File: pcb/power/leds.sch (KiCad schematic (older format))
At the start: 26 parts, among them U4 LM324QT

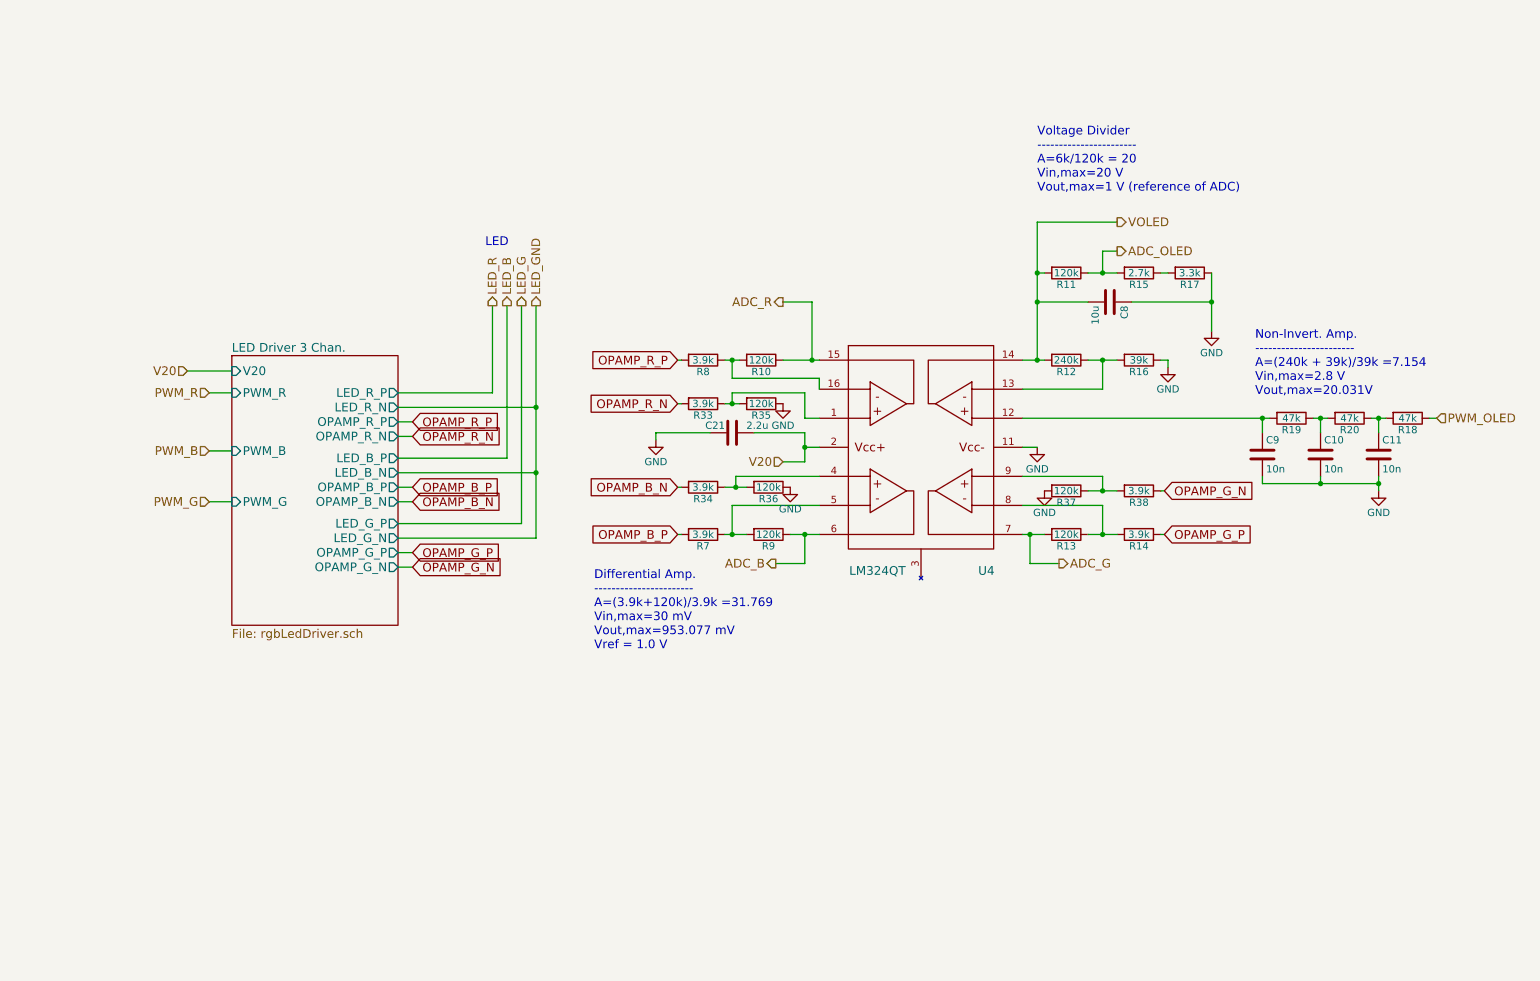
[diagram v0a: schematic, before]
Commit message: Almost finished the new schematics.
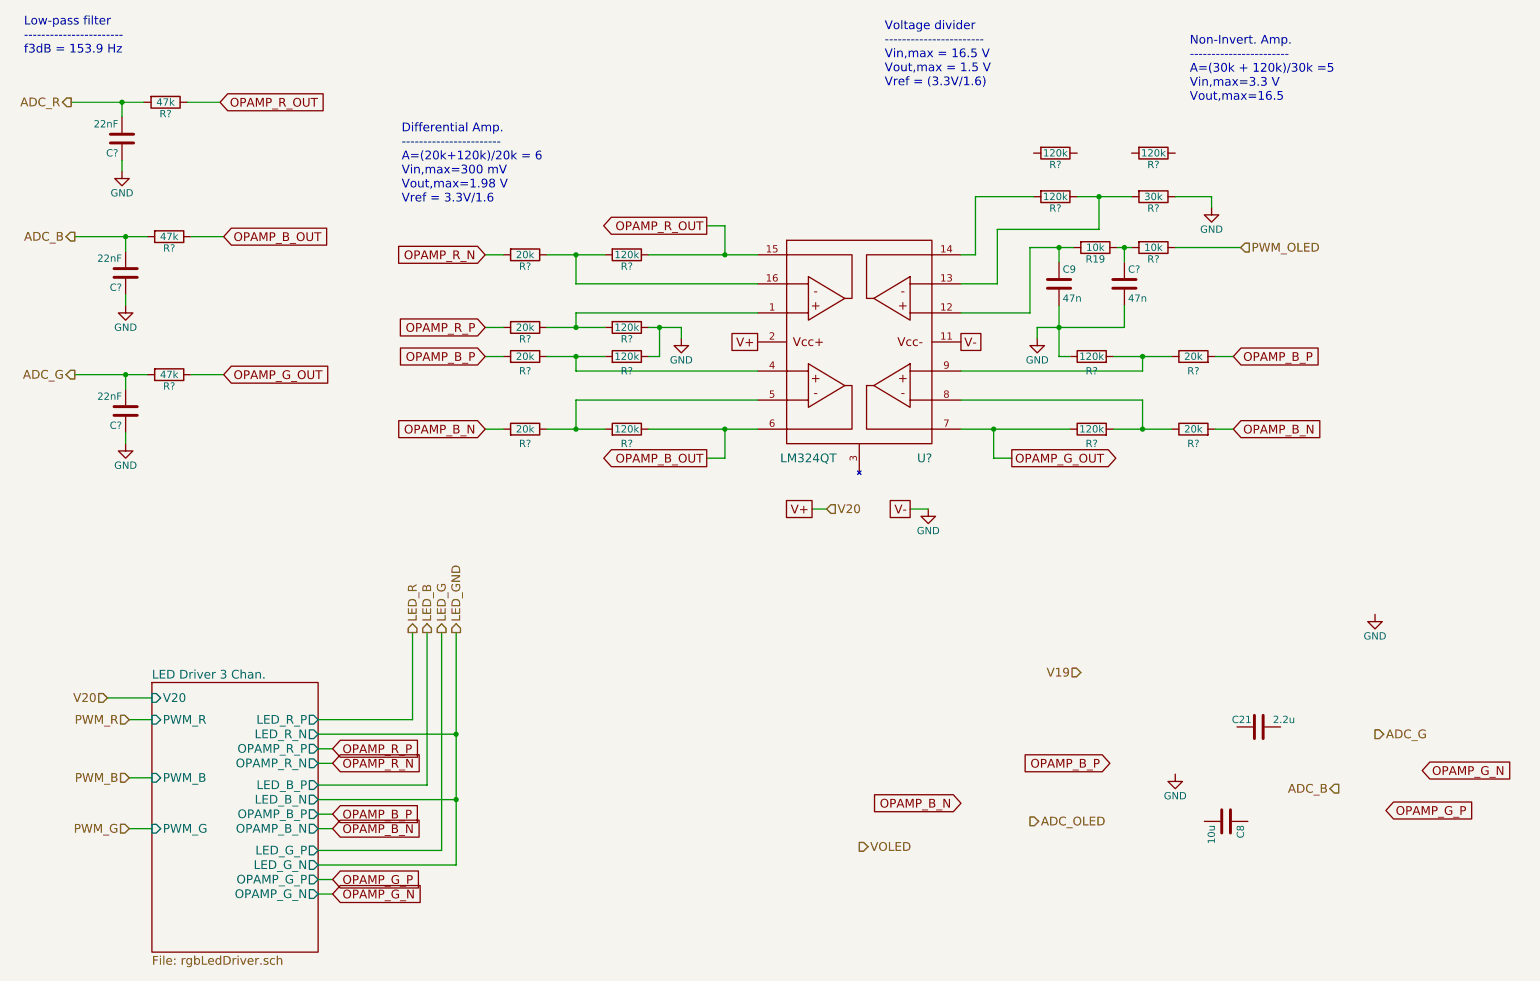
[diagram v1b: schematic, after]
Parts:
- removed C10, C11: 10n, Capacitors_SMD:C_0603_HandSoldering, symbol C
- removed R10, R11, R13, R35, R36, R37, R9: 120k, Additional:R_0603_HandSoldering_Same_As_C, symbol R
- removed R12: 240k, Additional:R_0603_HandSoldering_Same_As_C, symbol R
- removed R14, R33, R34, R38, R7, R8: 3.9k, Additional:R_0603_HandSoldering_Same_As_C, symbol R
- removed R15: 2.7k, Additional:R_0603_HandSoldering_Same_As_C, symbol R
- removed R16: 39k, Additional:R_0603_HandSoldering_Same_As_C, symbol R
- removed R17: 3.3k, Additional:R_0603_HandSoldering_Same_As_C, symbol R
- removed R18, R20: 47k, Additional:R_0603_HandSoldering_Same_As_C, symbol R
- removed U4: LM324QT, Additional:QFN-16-1EP_3x3mm_Pitch0.5mm, symbol LM324QT
- added C?: 47n, Capacitors_SMD:C_0603_HandSoldering, symbol C
- added C? (x3): 22nF, Capacitors_SMD:C_0603_HandSoldering, symbol C
- added R?: 10k, Additional:R_0603_HandSoldering_Same_As_C, symbol R
- added R? (x6): 20k, Additional:R_0603_HandSoldering_Same_As_C, symbol R
- added R? (x9): 120k, Additional:R_0603_HandSoldering_Same_As_C, symbol R
- added R? (x3): 47k, Additional:R_0603_HandSoldering_Same_As_C, symbol R
- added R?: 30k, Additional:R_0603_HandSoldering_Same_As_C, symbol R
- added U?: LM324QT, symbol LM324QT
- C9: value 10n -> 47n; Digikey 311-1085-1-ND -> (none); Farnell (none) -> 1759011
- R19: value 47k -> 10k; Digikey 311-47.0KHRCT-ND -> (none); Farnell (none) -> 2141505
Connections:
- net ADC_B: now also C?.2, R?.2
- net ADC_G: now also C?.2, R?.2
- net ADC_R: now also C?.2, R?.2
- net GND: now also C?.1, C?.1, C?.1, C?.2, R?.1, R?.1, R?.1, R?.1, U?.11 (Vcc-); no longer C21.1, C8.1
- net OPAMP_B_N: now also R?.2, R?.2
- net OPAMP_B_P: now also R?.2, R?.2
- net OPAMP_R_N: now also R?.2
- net OPAMP_R_P: now also R?.2
- net PWM_OLED: now also R?.1
- net VOLED: no longer C8.2
- net at C9.1, R19.2: now also U?.12 (P_4)
- net at R19.1: now also C?.1, R?.2
- net V20: no longer names the net of C21.2
- new net: R?.1, R?.2, U?.1 (P_1)
- new net: R?.1, R?.2, U?.13 (N_4)
- new net: R?.2, U?.14 (O_4)
- new net: R?.1, R?.2, U?.16 (N_1)
- new net: R?.1, R?.2, U?.4 (P_2)
- new net: R?.1, R?.2, U?.5 (N_2)
- new net: R?.1, R?.2, U?.8 (N_3)
- new net: R?.1, R?.2, U?.9 (P_3)
- new net OPAMP_B_OUT: R?.1, R?.1, U?.6 (O_2)
- new net OPAMP_G_OUT: R?.1, R?.1, U?.7 (O_3)
- new net OPAMP_R_OUT: R?.1, R?.1, U?.15 (O_1)
- new net V+: U?.2 (Vcc+)
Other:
- note added: "Differential Amp.\n-----------------------\nA=(20k+120k)/20k = 6\nVin,max=300 mV\nVout,max=1.98 V\nVref = 3.3V/1.6"
- note added: "Low-pass filter\n-----------------------\nf3dB = 153.9 Hz"
- note added: "Non-Invert. Amp.\n-----------------------\nA=(30k + 120k)/30k =5\nVin,max=3.3 V\nVout,max=16.5"
- note added: "Voltage divider\n-----------------------\nVin,max = 16.5 V\nVout,max = 1.5 V \nVref = (3.3V/1.6)"
- note removed: "Differential Amp.\n-----------------------\nA=(3.9k+120k)/3.9k =31.769\nVin,max=30 mV\nVout,max=953.077 mV\nVref = 1.0 V"
- note removed: "LED"
- note removed: "Non-Invert. Amp.\n-----------------------\nA=(240k + 39k)/39k =7.154\nVin,max=2.8 V\nVout,max=20.031V"
- note removed: "Voltage Divider\n-----------------------\nA=6k/120k = 20\nVin,max=20 V\nVout,max=1 V (reference of ADC)"
- moved on the sheet: C21, C8, C9, R19

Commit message: Produced gerber files.
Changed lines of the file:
@@
 $EndComp
 Wire Wire Line
-	8350 2300 8400 2300
-Wire Wire Line
-	8400 2300 8450 2300
+	8350 2300 8450 2300
 Wire Wire Line
 	8400 2850 8400 2700
@@
 	2850 5650 3800 5650
 Wire Wire Line
-	3800 4950 3800 5650
-Wire Wire Line
-	3800 5650 3800 6100
-Wire Wire Line
-	3800 6100 3800 6550
+	3800 4950 3800 6550
 Wire Wire Line
 	2850 6000 3600 6000
@@
 	8750 2300 9200 2300
 Wire Wire Line
-	4425 2350 4625 2350
-Wire Wire Line
-	4625 2350 4825 2350
+	4425 2350 4825 2350
 Connection ~ 4625 2350
 Wire Wire Line
-	4425 2850 4625 2850
-Wire Wire Line
-	4625 2850 4825 2850
+	4425 2850 4825 2850
 Wire Wire Line
 	4000 2350 4125 2350
@@
 	1500 1400 1500 1300
 Wire Wire Line
-	1150 1300 1500 1300
-Wire Wire Line
-	1500 1300 1650 1300
+	1150 1300 1650 1300
 Wire Wire Line
 	1500 1700 1500 1775
@@
 	1525 2325 1525 2225
 Wire Wire Line
-	1175 2225 1525 2225
-Wire Wire Line
-	1525 2225 1675 2225
+	1175 2225 1675 2225
 Wire Wire Line
 	1525 2625 1525 2700
@@
 	1525 3275 1525 3175
 Wire Wire Line
-	1175 3175 1525 3175
-Wire Wire Line
-	1525 3175 1675 3175
+	1175 3175 1675 3175
 Wire Wire Line
 	1525 3575 1525 3650
@@
 	4625 2350 4625 2550
 Wire Wire Line
-	5125 2350 5650 2350
-Wire Wire Line
-	5650 2350 5875 2350
+	5125 2350 5875 2350
 Wire Wire Line
 	5525 2150 5650 2150
@@
 Connection ~ 5650 2350
 Wire Wire Line
-	4425 3550 4625 3550
-Wire Wire Line
-	4625 3550 4825 3550
+	4425 3550 4825 3550
 Connection ~ 4625 3550
 Wire Wire Line
-	4425 3050 4625 3050
-Wire Wire Line
-	4625 3050 4825 3050
+	4425 3050 4825 3050
 Wire Wire Line
 	4000 3550 4125 3550
@@
 	4625 3550 4625 3350
 Wire Wire Line
-	5125 3550 5650 3550
-Wire Wire Line
-	5650 3550 5875 3550
+	5125 3550 5875 3550
 Wire Wire Line
 	5525 3750 5650 3750
@@
 Connection ~ 5650 3550
 Wire Wire Line
-	5125 2850 5200 2850
-Wire Wire Line
-	5200 2850 5350 2850
+	5125 2850 5350 2850
 Wire Wire Line
 	5350 2850 5350 2925
@@
 Connection ~ 5200 2850
 Wire Wire Line
-	8325 3550 8525 3550
-Wire Wire Line
-	8525 3550 8725 3550
+	8325 3550 8725 3550
 Connection ~ 8525 3550
 Wire Wire Line
-	8325 3050 8525 3050
-Wire Wire Line
-	8525 3050 8725 3050
+	8325 3050 8725 3050
 Wire Wire Line
 	9150 3550 9025 3550
@@
 	8525 3550 8525 3350
 Wire Wire Line
-	7275 3550 7500 3550
-Wire Wire Line
-	7500 3550 8025 3550
+	7275 3550 8025 3550
 Wire Wire Line
 	7625 3750 7500 3750
@@
 	7750 2750 7750 2300
 Wire Wire Line
-	7750 2300 7950 2300
-Wire Wire Line
-	7950 2300 8050 2300
+	7750 2300 8050 2300
 Wire Wire Line
 	7950 2400 7950 2300
@@
 Connection ~ 7950 2850
 Wire Wire Line
-	7950 2700 7950 2850
-Wire Wire Line
-	7950 2850 7950 3050
+	7950 2700 7950 3050
 $Comp
 L R R?
@@
 	7375 1950 7775 1950
 Wire Wire Line
-	8075 1950 8225 1950
-Wire Wire Line
-	8225 1950 8450 1950
+	8075 1950 8450 1950
 Wire Wire Line
 	8750 1950 9000 1950
@@
 	7375 2350 7375 1950
 Wire Wire Line
-	7800 2850 7950 2850
-Wire Wire Line
-	7950 2850 8400 2850
+	7800 2850 8400 2850
 Text GLabel 7275 2950 2    60   UnSpc ~ 0
 V-
